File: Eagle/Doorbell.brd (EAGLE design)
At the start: 36.1 x 28.7 mm, 31 parts, among them U1 MIC2920A-3.3

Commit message: r1 - switching supply
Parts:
- removed C5: 470uF 25V, SparkFun-Capacitors:PANASONIC_E
- removed U1: MIC2920A-3.3, Microchip_By_element14_Batch_1:SOT230P700X180-4N
- added C8: 2.2uF, SparkFun-Passives:1206
- added D5: BAT20J, SparkFun-DiscreteSemi:SOD-323
- added L1: 6.8uH, SparkFun-Passives:1007
- added VREG: LMR16006YQ3DDCRQ1, CuriousTech:SOT-23-6
- C1: value 0.1uF -> 10uF
- C4: value 10uF 16V -> 100uF; device SparkFun-Capacitors:PANASONIC_C -> SparkFun-Passives:NIPPON_F80
- R4: value 5K6 -> 470
- moved C3 10.2 mm to (32.0, 1.52), turned to 0 degrees
- moved C4 8.89 mm to (31.8, 8.38), turned to 180 degrees
- moved C6 5.43 mm to (23.4, 5.64), turned to 270 degrees
- moved C1 3.38 mm to (20.9, 10.5)
- moved C7 1.70 mm to (20.1, 5.59), turned to 0 degrees
- moved D2 0.76 mm to (26.4, 16.3)
- moved D3 0.51 mm to (26.4, 18.5)
- moved D1 0.25 mm to (26.4, 20.8)
- moved D4 0.25 mm to (26.4, 23.4)
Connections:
- removed net N$1: C3.1, C5.+, C6.1, D1.C, D3.C, U1.1
- new net +24V: C3.1, C4.+, C8.1, D1.C, D3.C, VREG.5
- new net N$10: C6.2, VREG.1
- new net N$7: C6.1, D5.C, L1.1, VREG.6
- net 3V3: now also L1.2, VREG.3; no longer C4.+, U1.3
- net GND: now also C8.2, D5.A, VREG.2; no longer C5.-, C6.2, U1.2, U1.4
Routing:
- net +24V: track 0.00 -> 29.8 mm, vias 0 -> 1
- net N$1: track 26.0 -> 0.00 mm, vias 2 -> 0
- net N$7: track 0.00 -> 9.21 mm
- net 3V3: track 59.2 -> 64.0 mm, vias 1 -> 0
- net GND: track 0.00 -> 2.40 mm
- net N$10: track 0.00 -> 2.00 mm

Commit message: Add files via upload
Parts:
- removed X1: (no value), con-molex:KK-156-4
- added 3V3: MCP1755T-3302E/OT, Microchip_By_element14_Batch_1:SOT95P270X145-5N
- added C5: 0.1uF, SparkFun-Capacitors:0805-CAP
- added D6, D7: (no value), SparkFun-DiscreteSemi:SOD-123
- added J2, J3: (no value), SparkFun-Connectors:1X01NS
- added L2: (no value), SparkFun-Passives:0805
- added Q1: MOSFET-NCHANNEL, SparkFun-DiscreteSemi:SOT23-3
- added R9: 1K, SparkFun-Resistors:0805
- added U$6, U$7: SMD-PAD-SM, CuriousTech:SMD-PAD3
- added X2: 1751251, con-phoenix-350:1751251
- C1: value 10uF -> (none); device SparkFun-Capacitors:0805-CAP -> SparkFun-Capacitors:CPOL-RADIAL-1000UF-25V
- C2: value 1uF -> 2.2uF; device SparkFun-Capacitors:0805-CAP -> SparkFun-Passives:1206
- C3: value 0.1uF -> 10uF
- C4: value 100uF -> 0.1uF; device SparkFun-Passives:NIPPON_F80 -> SparkFun-Capacitors:0805-CAP
- C8: value 2.2uF -> 1uF; device SparkFun-Passives:1206 -> SparkFun-Capacitors:0805-CAP
- L1: value 6.8uH -> (none); device SparkFun-Passives:1007 -> SparkFun-Passives:0805
- R4: value 470 -> 1K
- R5, R6: value 10K -> 4K7
- VREG: value LMR16006YQ3DDCRQ1 -> LMR16006YQ5DDCRQ1
- moved C8 25.4 mm to (21.3, 26.7), turned to 180 degrees
- moved C2 25.2 mm to (32.9, 5.03), turned to 0 degrees
- moved U$3 14.0 mm to (23.9, 25.7)
- moved C3 13.5 mm to (23.6, 12.0)
- moved C1 10.0 mm to (30.7, 12.2), turned to 270 degrees
- moved C7 8.13 mm to (20.3, 13.7), turned to 180 degrees
- moved C4 6.12 mm to (32.3, 2.29), turned to 0 degrees
- moved U$4 5.84 mm to (9.91, 25.7)
- moved L1 2.76 mm to (26.4, 8.13), turned to 90 degrees
- moved D5 2.70 mm to (28.2, 5.11), turned to 0 degrees
- moved D2 2.54 mm to (24.4, 17.8), turned to 90 degrees
- moved D1 2.09 mm to (26.9, 22.9), turned to 90 degrees
- moved D4 2.09 mm to (24.4, 22.9), turned to 270 degrees
- moved R5 2.03 mm to (14.7, 5.84)
- moved R6 1.78 mm to (12.2, 5.84)
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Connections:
- net IO5 renamed DB
- new net 5V: 3V3.1, 3V3.3, C3.1, C7.1, D6.C, L1.2, L2.2, U$7.P$1, VREG.3, _.8
- new net N$1: D6.A, D7.A, Q1.3, U$6.P$1
- new net N$8: Q1.1, R9.2
- net +24V: now also C1.+, C2.1, C4.1, D7.C, U$3.P$1; no longer C3.1, C4.+, C8.1
- net 3V3: now also 3V3.5, C5.1, _.7; no longer C1.1, C7.1, L1.2, U$3.P$1, VREG.3, _.6, _.8
- net GND: now also 3V3.2, C1.-, C2.2, C4.2, C5.2, Q1.2, _.3; no longer C1.2, C4.-, C8.2, _.7
- net IO12: now also _.5; no longer _.4
- net IO13: now also _.6; no longer _.5
- net IO14: now also _.4; no longer _.3
- net IO15: now also R9.1
- net J1: now also C8.2, X2.2; no longer C2.2, X1.3
- net N$2: now also C8.1; no longer C2.1
- net N$3: now also J2.1, X2.1; no longer X1.1, X1.2
- net N$5: now also J3.1, X2.3; no longer X1.4
- net N$7: now also L2.1
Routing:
- net 5V: track 0.00 -> 49.3 mm, vias 0 -> 1
- net 3V3: track 64.0 -> 32.8 mm
- net +24V: track 29.8 -> 41.0 mm
- net N$1: track 0.00 -> 9.34 mm
- net IO15: track 3.47 -> 7.56 mm
- net N$8: track 0.00 -> 3.09 mm, vias 0 -> 1
- net J1: track 20.0 -> 17.1 mm
- net DB: track 16.9 -> 18.6 mm
- net IO14: track 6.26 -> 4.77 mm
- net IO12: track 8.96 -> 7.64 mm
- net N$5: track 6.34 -> 7.07 mm
- net GND: track 2.40 -> 2.30 mm, vias 2 -> 1
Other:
- board size 36.1 x 28.7 mm -> 35.8 x 28.7 mm
- board text added: "24V"
- board text added: "5V"
- board text added: "Btn"
- board text added: "GND"
- board text added: "GND ADC GND 14 12 13 3V3 5V"
- board text added: "SPK"
- board text added: "TF"
- board text removed: "3V3"
- board text removed: "Btn-DB"
- board text removed: "GND ADC 14 12 13 3v3 GND 3v3"
- board text removed: "TF-DB"

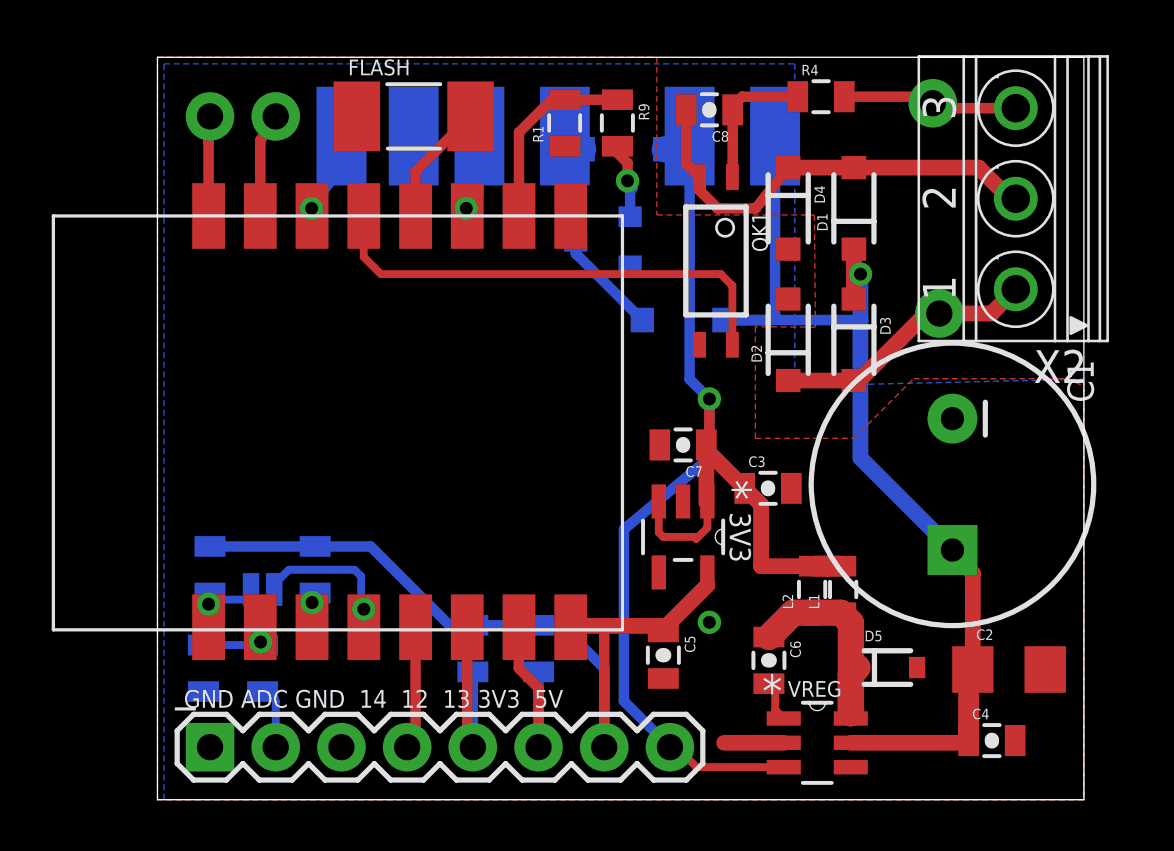
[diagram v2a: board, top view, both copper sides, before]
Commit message: Added the inline diode
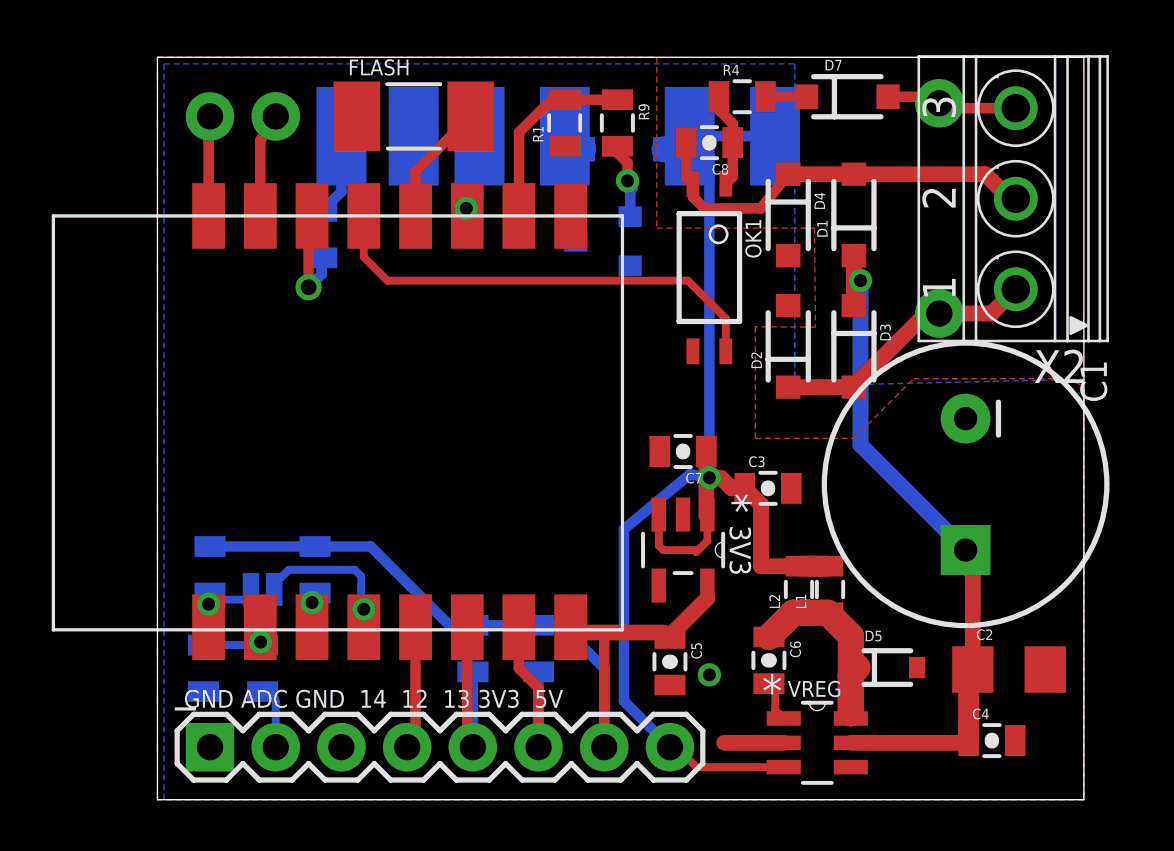
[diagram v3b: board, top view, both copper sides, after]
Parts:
- added R10: 470, SparkFun-Resistors:0805
- R4: value 1K -> 2K2
- moved D7 10.7 mm to (26.7, 27.2), flipped to the top
- moved R4 3.05 mm to (22.6, 27.2)
- moved C8 1.27 mm to (21.3, 25.4)
- moved 3V3 0.51 mm to (20.3, 9.65)
- moved C1 0.51 mm to (31.2, 12.2)
- moved L1 0.51 mm to (25.9, 8.13)
- moved L2 0.51 mm to (24.9, 8.13)
- moved C5 0.36 mm to (19.8, 5.33)
- moved OK1 0.36 mm to (21.3, 20.6)
- moved D2 0.25 mm to (24.4, 17.5)
- moved D3 0.25 mm to (26.9, 17.5)
- moved C7 0.25 mm to (20.3, 13.5)
- moved D1 0.25 mm to (26.9, 22.6)
- moved D4 0.25 mm to (24.4, 22.6)
- moved J3 0.25 mm to (30.2, 26.9)
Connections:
- new net N$12: R10.2, U$2.P$1
- new net N$13: D7.C, R4.2
- net +24V: no longer D7.C, U$3.P$1
- net 5V: now also U$3.P$1
- net N$1: no longer D7.A
- net N$5: now also D7.A; no longer R4.2
- net N$6: now also R10.1; no longer U$2.P$1
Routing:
- net +24V: track 41.0 -> 27.2 mm
- net N$1: track 9.34 -> 5.23 mm
- net N$12: track 0.00 -> 3.23 mm
- net 5V: track 49.3 -> 52.5 mm
- net N$2: track 5.42 -> 3.69 mm
- net N$13: track 0.00 -> 1.59 mm
- net N$5: track 7.07 -> 5.74 mm
- net J1: track 17.1 -> 15.9 mm
- net DB: track 18.6 -> 17.8 mm
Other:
- board text removed: "24V"
